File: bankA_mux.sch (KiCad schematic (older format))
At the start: 7 parts, among them U10 SHIFTER, U9 74HC4051

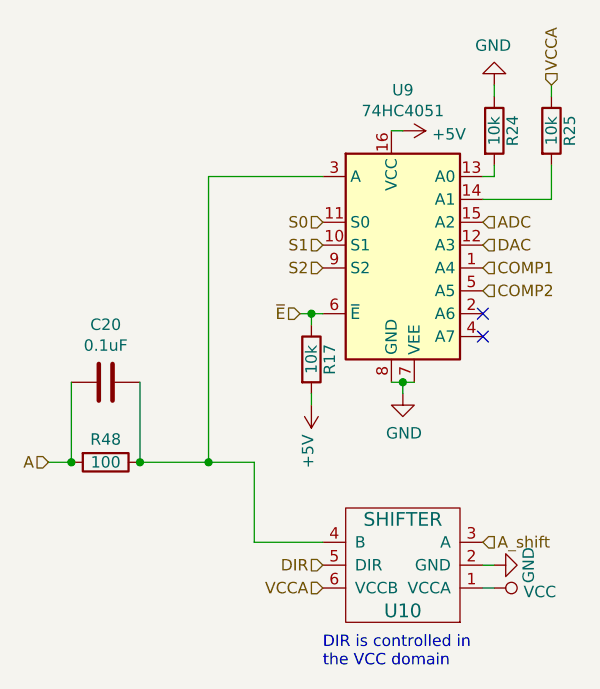
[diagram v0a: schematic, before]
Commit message: Improved silkscreen table visibility and changed board edge cuts to support right-angle connectors
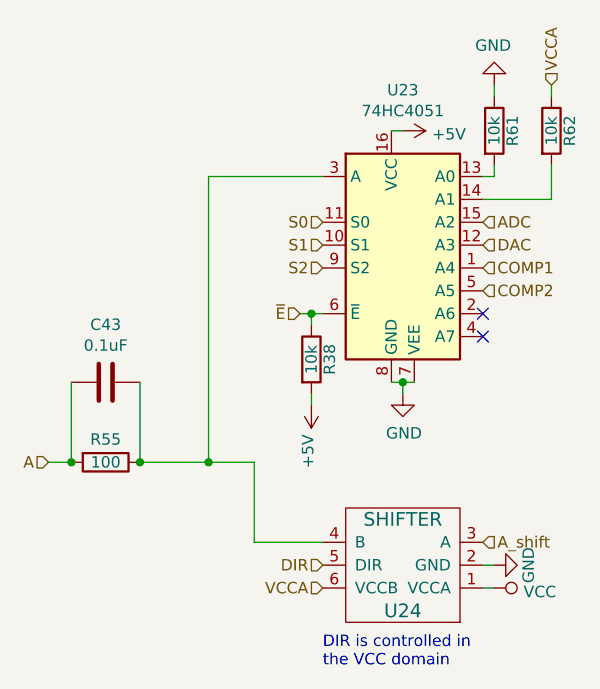
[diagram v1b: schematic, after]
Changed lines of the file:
@@
 AR Path="/5D1A4680/5CF3E254" Ref="U21"  Part="1"
 AR Path="/5D1A4696/5CF3E254" Ref="U23"  Part="1"
-F 0 "U9" H 4100 3428 50  0000 C CNN
+F 0 "U23" H 4100 3428 50  0000 C CNN
 F 1 "74HC4051" H 4100 3337 50  0000 C CNN
 F 2 "Package_TO_SOT_SMD:SOT-763-1" H 4050 2350 50  0001 C CNN
@@
 AR Path="/5D1A4680/5CF3E28C" Ref="U22"  Part="1"
 AR Path="/5D1A4696/5CF3E28C" Ref="U24"  Part="1"
-F 0 "U10" H 4100 4350 60  0000 C CNN
+F 0 "U24" H 4100 4350 60  0000 C CNN
 F 1 "SHIFTER" H 4100 3950 60  0000 C CNN
 F 2 "gsg-modules:SOT363" H 4100 4150 60  0001 C CNN
@@
 AR Path="/5D190D22/5CB0C423" Ref="R51"  Part="1"
 AR Path="/5D1A466A/5CB0C423" Ref="R53"  Part="1"
-F 0 "R48" V 2700 3700 50  0000 C CNN
+F 0 "R55" V 2700 3700 50  0000 C CNN
 F 1 "100" V 2800 3700 50  0000 C CNN
 F 2 "gsg-modules:0402" V 2730 3700 50  0001 C CNN
@@
 AR Path="/5D1A4680/5CDC112C" Ref="R47"  Part="1"
 AR Path="/5D1A4696/5CDC112C" Ref="R62"  Part="1"
-F 0 "R25" V 4830 2250 50  0000 C CNN
+F 0 "R62" V 4830 2250 50  0000 C CNN
 F 1 "10k" V 4750 2250 50  0000 C CNN
 F 2 "gsg-modules:0402" V 4680 2250 50  0001 C CNN
@@
 AR Path="/5D1A4680/5D112AA5" Ref="C42"  Part="1"
 AR Path="/5D1A4696/5D112AA5" Ref="C43"  Part="1"
-F 0 "C20" V 3052 3350 50  0000 C CNN
+F 0 "C43" V 3052 3350 50  0000 C CNN
 F 1 "0.1uF" V 2961 3350 50  0000 C CNN
 F 2 "gsg-modules:0402" H 2838 3200 50  0001 C CNN
@@
 AR Path="/5D1A4680/5D2823C8" Ref="R46"  Part="1"
 AR Path="/5D1A4696/5D2823C8" Ref="R61"  Part="1"
-F 0 "R24" V 4580 2250 50  0000 C CNN
+F 0 "R61" V 4580 2250 50  0000 C CNN
 F 1 "10k" V 4500 2250 50  0000 C CNN
 F 2 "gsg-modules:0402" V 4430 2250 50  0001 C CNN
@@
 AR Path="/5D1A4680/5D2825B7" Ref="R35"  Part="1"
 AR Path="/5D1A4696/5D2825B7" Ref="R38"  Part="1"
-F 0 "R17" V 3780 3250 50  0000 C CNN
+F 0 "R38" V 3780 3250 50  0000 C CNN
 F 1 "10k" V 3700 3250 50  0000 C CNN
 F 2 "gsg-modules:0402" V 3630 3250 50  0001 C CNN

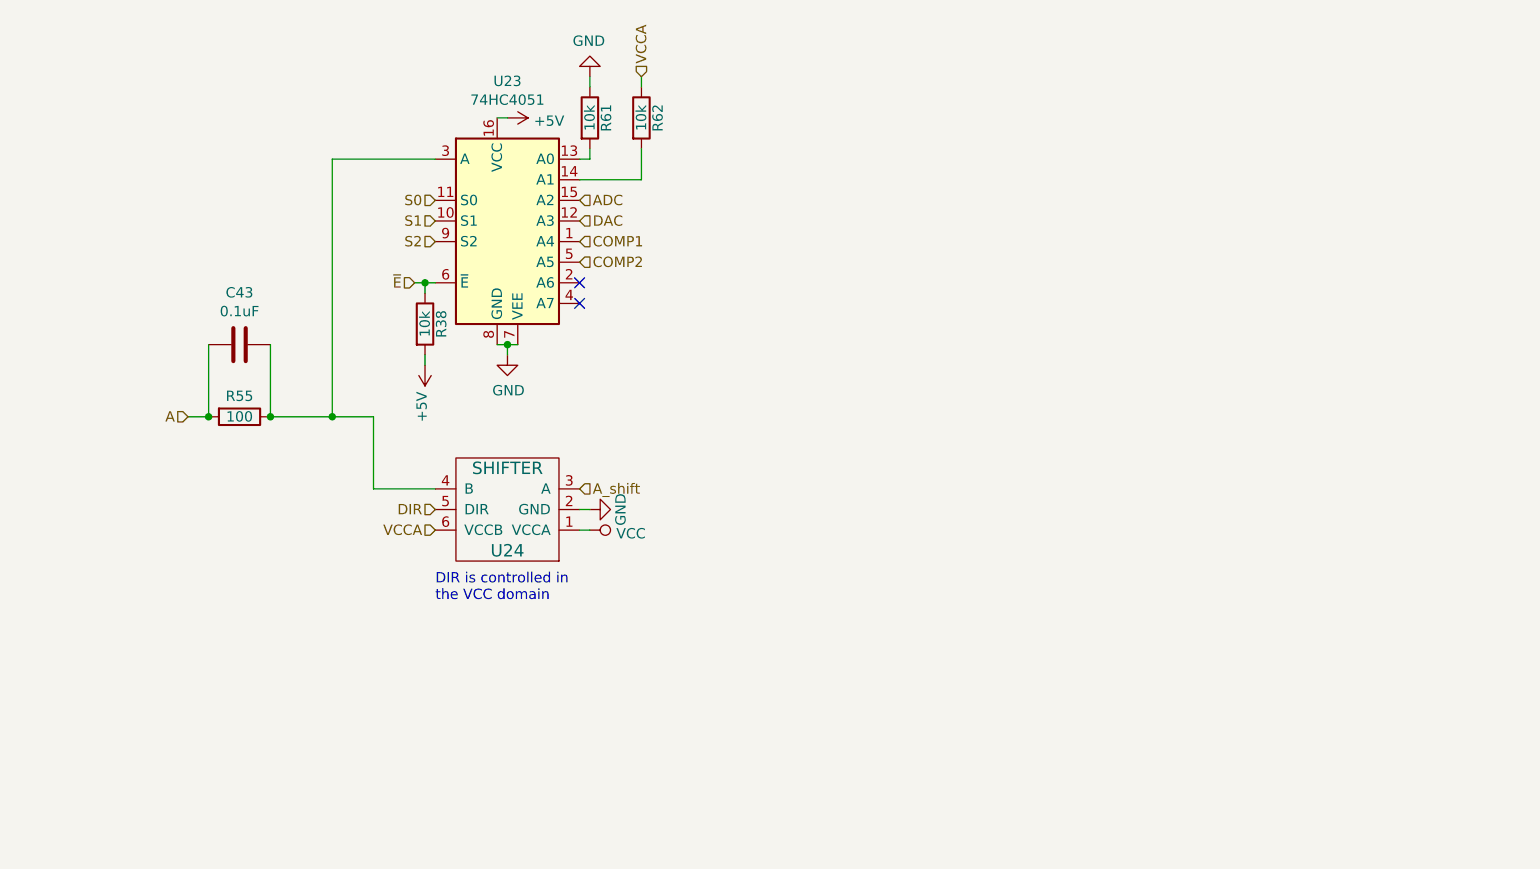
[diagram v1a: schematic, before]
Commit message: schematic: cleanup and squish onto a page
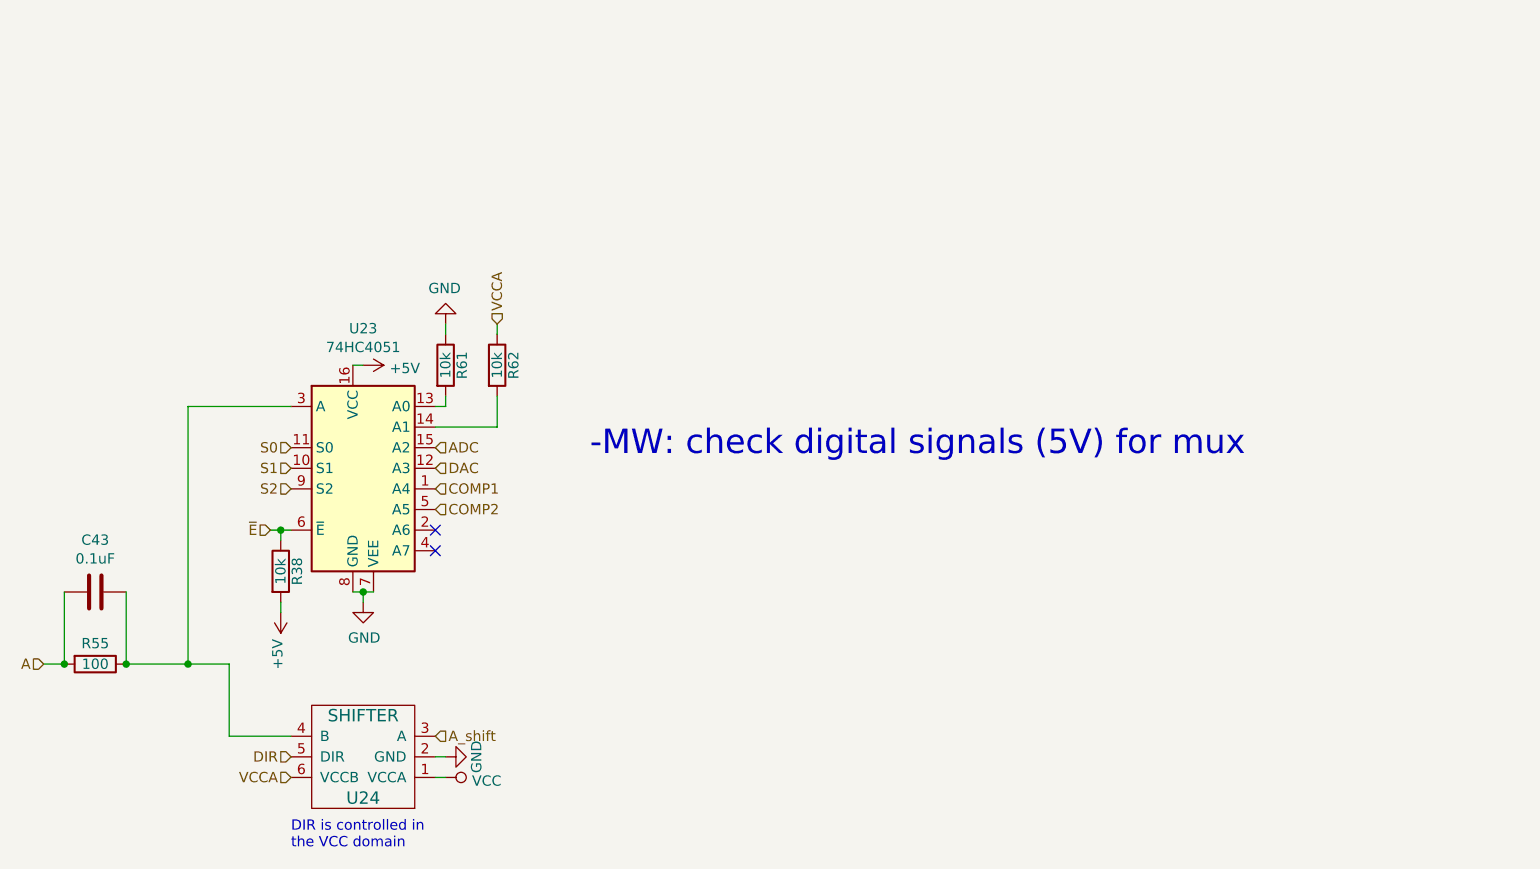
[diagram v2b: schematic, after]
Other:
- note added: "-MW: check digital signals (5V) for mux"
- moved on the sheet: C43, R38, R55, R61, R62, U23, U24
